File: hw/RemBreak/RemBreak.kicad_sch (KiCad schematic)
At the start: 6 parts, among them J2 Conn_02x06_Odd_Even

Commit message: updated pcb and schematics - still in progress
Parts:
- removed R3: 0R, Resistor_SMD:R_0805_2012Metric, symbol Device:R
- added J3, J5: Screw_Terminal_01x04, TerminalBlock_Phoenix:TerminalBlock_Phoenix_MPT-0,5-4-2.54_1x04_P2.54mm_Horizontal, symbol Connector:Screw_Terminal_01x04
- J2: footprint Connector_PinHeader_2.54mm:PinHeader_2x06_P2.54mm_Vertical_SMD -> dodo_conn:SAMTEC_TSM-106-01-L-DH-P-TR
- R1: now not fitted
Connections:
- net GND: now also J2.11 (Pin_11), J2.12 (Pin_12), J2.7 (Pin_7), J2.8 (Pin_8), J3.4 (Pin_4), J5.2 (Pin_2), J5.4 (Pin_4)
- net 7V5: now reaches R1.1
- net 7V5: now also J5.1 (Pin_1)
- net at R1.2: now also R2.2, J3.1 (Pin_1)
- net VEXT: now reaches R2.1
- net VEXT: now also J5.3 (Pin_3)
- net 3V3: now reaches J2.1 (Pin_1)
- net SCL: now reaches J2.10 (Pin_10)
- net 5V: now reaches J2.2 (Pin_2)
- net SW+: now reaches J2.3 (Pin_3)
- net SW-: now reaches J2.4 (Pin_4)
- net DISP_DCKI: now reaches J2.5 (Pin_5)
- net DISP_DI: now reaches J2.6 (Pin_6)
- net SDA: now reaches J2.9 (Pin_9)
- new net BUTTON: J3.3 (Pin_3)
- new net BUZZER: J3.2 (Pin_2)
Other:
- note removed: "HANDLEBARS + BOOST CONVERTER (12V)"
- note removed: "SERVO"
- moved on the sheet: J2

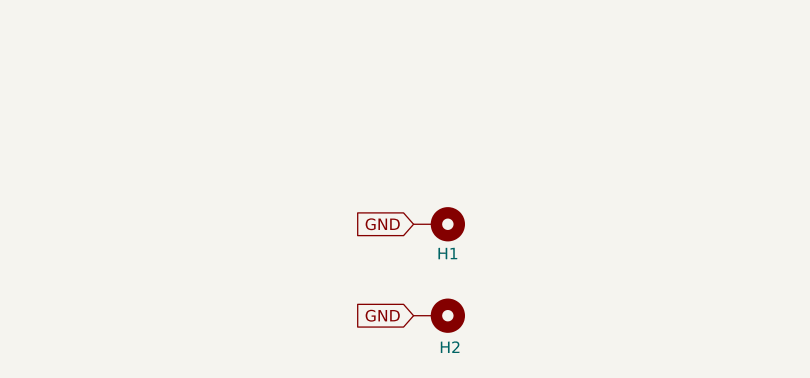
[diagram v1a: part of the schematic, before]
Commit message: changed size of the board and development of schematic
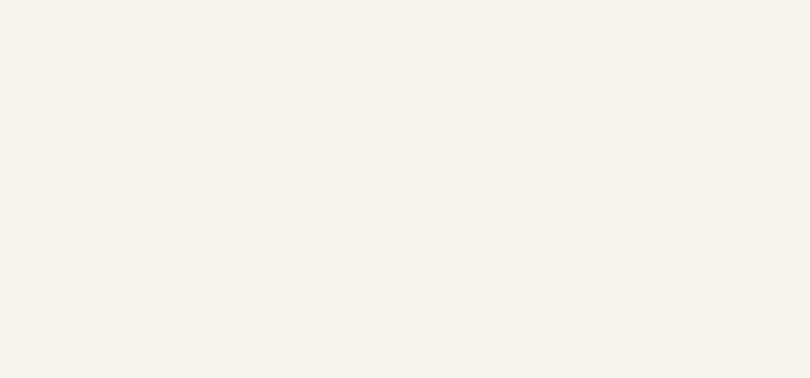
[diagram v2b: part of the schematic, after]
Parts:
- removed H1, H2: MountingHole_Pad, TestPoint:TestPoint_THTPad_2.0x2.0mm_Drill1.0mm, symbol Mechanical:MountingHole_Pad
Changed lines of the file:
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@@
-		)
-	)
-	(global_label "GND"
-		(shape input)
-		(at 153.67 175.26 180)
-		(fields_autoplaced yes)
-		(effects
-			(font
-				(size 1.27 1.27)
-			)
-			(justify right)
-		)
-		(property "Intersheetrefs" "${INTERSHEET_REFS}"
-			(at 146.8143 175.26 0)
-			(effects
-				(font
-					(size 1.27 1.27)
-				)
-				(justify right)
-				(hide yes)
-			)
-		)
-	)
-	(global_label "GND"
-		(shape input)
-		(at 153.67 185.42 180)
-		(fields_autoplaced yes)
-		(effects
-			(font
-				(size 1.27 1.27)
-			)
-			(justify right)
-		)
-		(property "Intersheetrefs" "${INTERSHEET_REFS}"
-			(at 146.8143 185.42 0)
-			(effects
-				(font
-					(size 1.27 1.27)
-				)
-				(justify right)
-				(hide yes)
-			)
 		)
 	)
@@
 	)
 	(symbol
-		(lib_id "Mechanical:MountingHole_Pad")
-		(at 156.21 175.26 270)
-		(unit 1)
-		(exclude_from_sim no)
-		(in_bom yes)
-		(on_board yes)
-		(dnp no)
-		(property "Reference" "H1"
-			(at 157.48 178.562 90)
-			(effects
-				(font
-					(size 1.27 1.27)
-				)
-			)
-		)
-		(property "Value" "MountingHole_Pad"
-			(at 157.48 179.07 90)
-			(effects
-				(font
-					(size 1.27 1.27)
-				)
-				(hide yes)
-			)
-		)
-		(property "Footprint" "TestPoint:TestPoint_THTPad_2.0x2.0mm_Drill1.0mm"
-			(at 156.21 175.26 0)
-			(effects
-				(font
-					(size 1.27 1.27)
-				)
-				(hide yes)
-			)
-		)
-		(property "Datasheet" "~"
-			(at 156.21 175.26 0)
-			(effects
-				(font
-					(size 1.27 1.27)
-				)
-				(hide yes)
-			)
-		)
-		(property "Description" "Mounting Hole with connection"
-			(at 156.21 175.26 0)
-			(effects
-				(font
-					(size 1.27 1.27)
-				)
-				(hide yes)
-			)
-		)
-		(pin "1"
-		)
-		(instances
-			(project "RemBreak"
-				(path "/e6d4ae5b-c9d7-4cbe-b288-c929fdf55a75"
-					(reference "H1")
-					(unit 1)
-				)
-			)
-		)
-	)
-	(symbol
 		(lib_id "Connector:Screw_Terminal_01x04")
 		(at 237.49 74.93 0)
@@
 					(unit 1)
 				)
-			)
-		)
-	)
-	(symbol
-		(lib_id "Mechanical:MountingHole_Pad")
-		(at 156.21 185.42 270)
-		(unit 1)
-		(exclude_from_sim no)
-		(in_bom yes)
-		(on_board yes)
-		(dnp no)
-		(property "Reference" "H2"
-			(at 157.734 188.976 90)
-			(effects
-				(font
-					(size 1.27 1.27)
-				)
-			)
-		)
-		(property "Value" "MountingHole_Pad"
-			(at 157.48 189.23 90)
-			(effects
-				(font
-					(size 1.27 1.27)
-				)
-				(hide yes)
-			)
-		)
-		(property "Footprint" "TestPoint:TestPoint_THTPad_2.0x2.0mm_Drill1.0mm"
-			(at 156.21 185.42 0)
-			(effects
-				(font
-					(size 1.27 1.27)
-				)
-				(hide yes)
-			)
-		)
-		(property "Datasheet" "~"
-			(at 156.21 185.42 0)
-			(effects
-				(font
-					(size 1.27 1.27)
-				)
-				(hide yes)
-			)
-		)
-		(property "Description" "Mounting Hole with connection"
-			(at 156.21 185.42 0)
-			(effects
-				(font
-					(size 1.27 1.27)
-				)
-				(hide yes)
-			)
-		)
-		(pin "1"
-		)
-		(instances
-			(project ""
-				(path "/e6d4ae5b-c9d7-4cbe-b288-c929fdf55a75"
-					(reference "H2")
-					(unit 1)
-				)

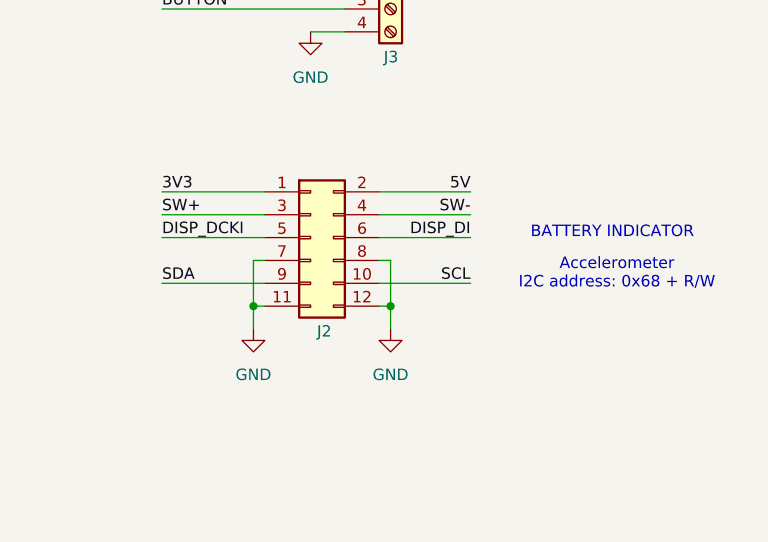
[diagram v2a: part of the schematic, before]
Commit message: added RGB LED connection - missing connections in schematics
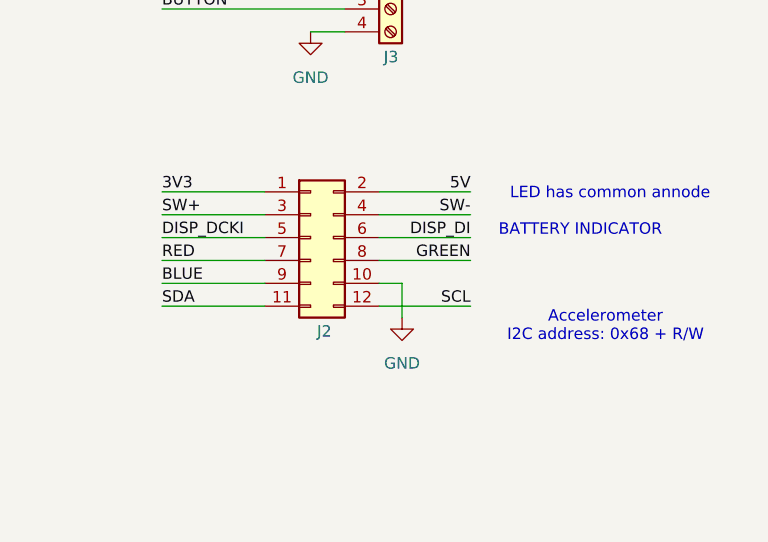
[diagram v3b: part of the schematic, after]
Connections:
- net GND: now also J2.10 (Pin_10); no longer J2.11 (Pin_11), J2.12 (Pin_12), J2.7 (Pin_7), J2.8 (Pin_8)
- net SCL: now also J2.12 (Pin_12); no longer J2.10 (Pin_10)
- net SDA: now also J2.11 (Pin_11); no longer J2.9 (Pin_9)
- new net BLUE: J2.9 (Pin_9)
- new net GREEN: J2.8 (Pin_8)
- new net RED: J2.7 (Pin_7)
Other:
- note added: "LED has common annode"

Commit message: finished schematics routing and erc passed
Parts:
- J2: footprint dodo_conn:SAMTEC_TSM-106-01-L-DH-P-TR -> chinese_modules:SAMTEC_TSM-106-01-L-DH-P-TR
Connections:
- net BUTTON is gone; now on net break_control/BUTTON: J3.3 (Pin_3)
- net SW+ is gone; now on net power_manager/VBATT: J2.3 (Pin_3)
- net 3V3 renamed +3V3
- net 5V renamed +5V
- net 7V5 renamed +7.5V
- net BLUE renamed power_manager/CHARGED (GREEN)
- net BUZZER renamed break_control/BUZZER
- net DISP_DCKI renamed DISPLAY.DCKI
- net DISP_DI renamed DISPLAY.DI
- net GREEN renamed power_switch/RUNNIG (RED)
- net RED renamed break_control/CHARGING
- net SCL renamed I2C.SCL
- net SDA renamed I2C.SDA
- net SW- renamed power_switch/ON/OFF
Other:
- sheet break_control ports: added BALARM, BUZZER, CHARGING, DISPLAY{DCKI DI}, I2C{SDA SCL}; removed I2C, PWR
- sheet power_manager ports: added BALARM, CHARGED (GREEN), CHARGING (BLUE), I2C{SDA SCL}, VBUS; removed 3V3, I2C
- sheet power_switch ports: added ON/OFF, RUNNIG (RED); removed PWR
- note added: "Potentially connect MPU6050 I2C address: 0x68 + R/W"
- note removed: "Accelerometer I2C address: 0x68 + R/W"
- note removed: "LED has common annode"
- moved on the sheet: J2, J3, J5, R1, R2

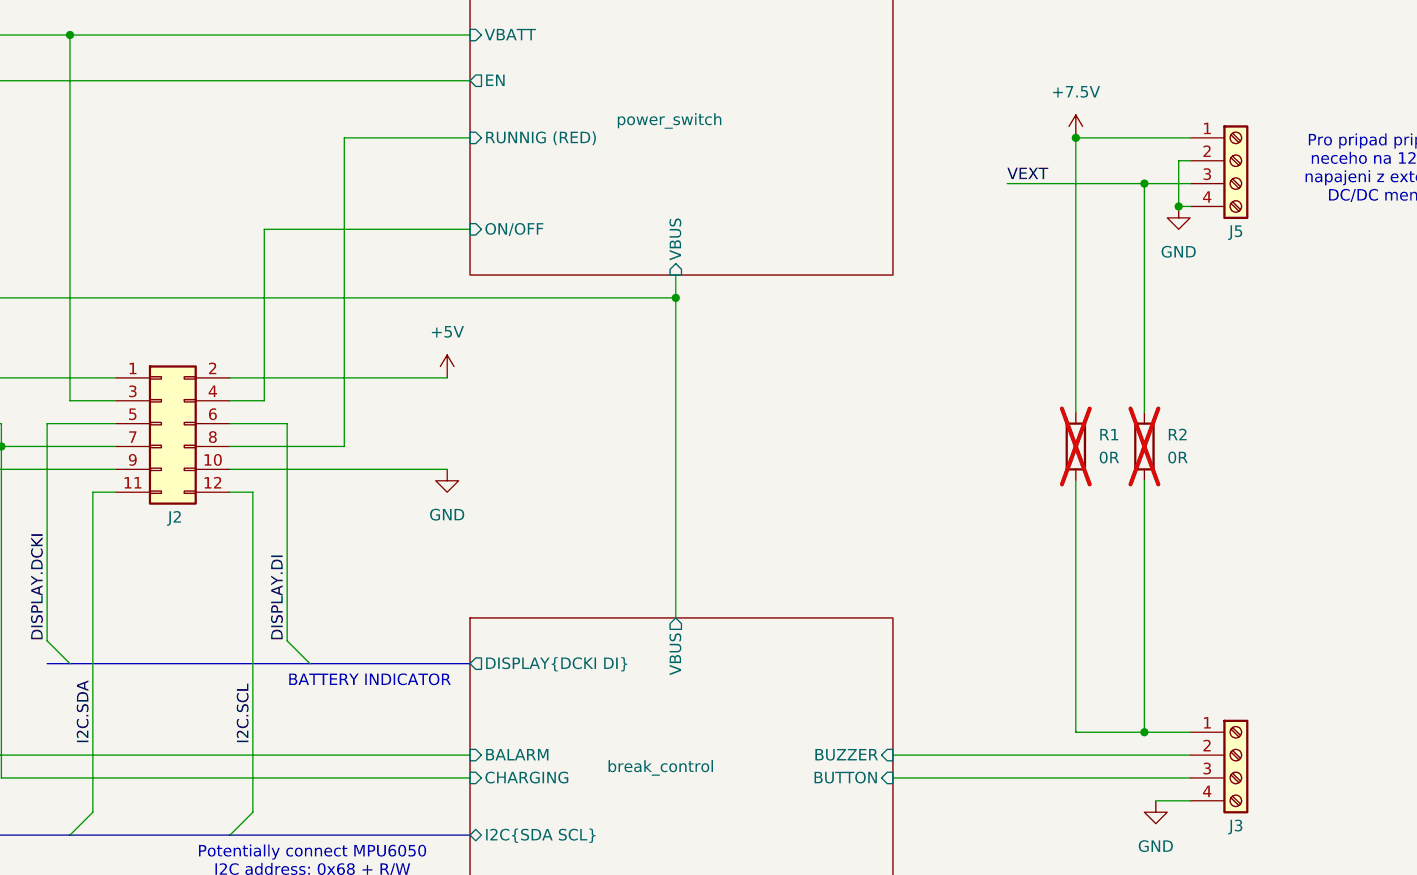
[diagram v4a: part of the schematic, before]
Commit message: regenerated anotations and used battery connector with grounding
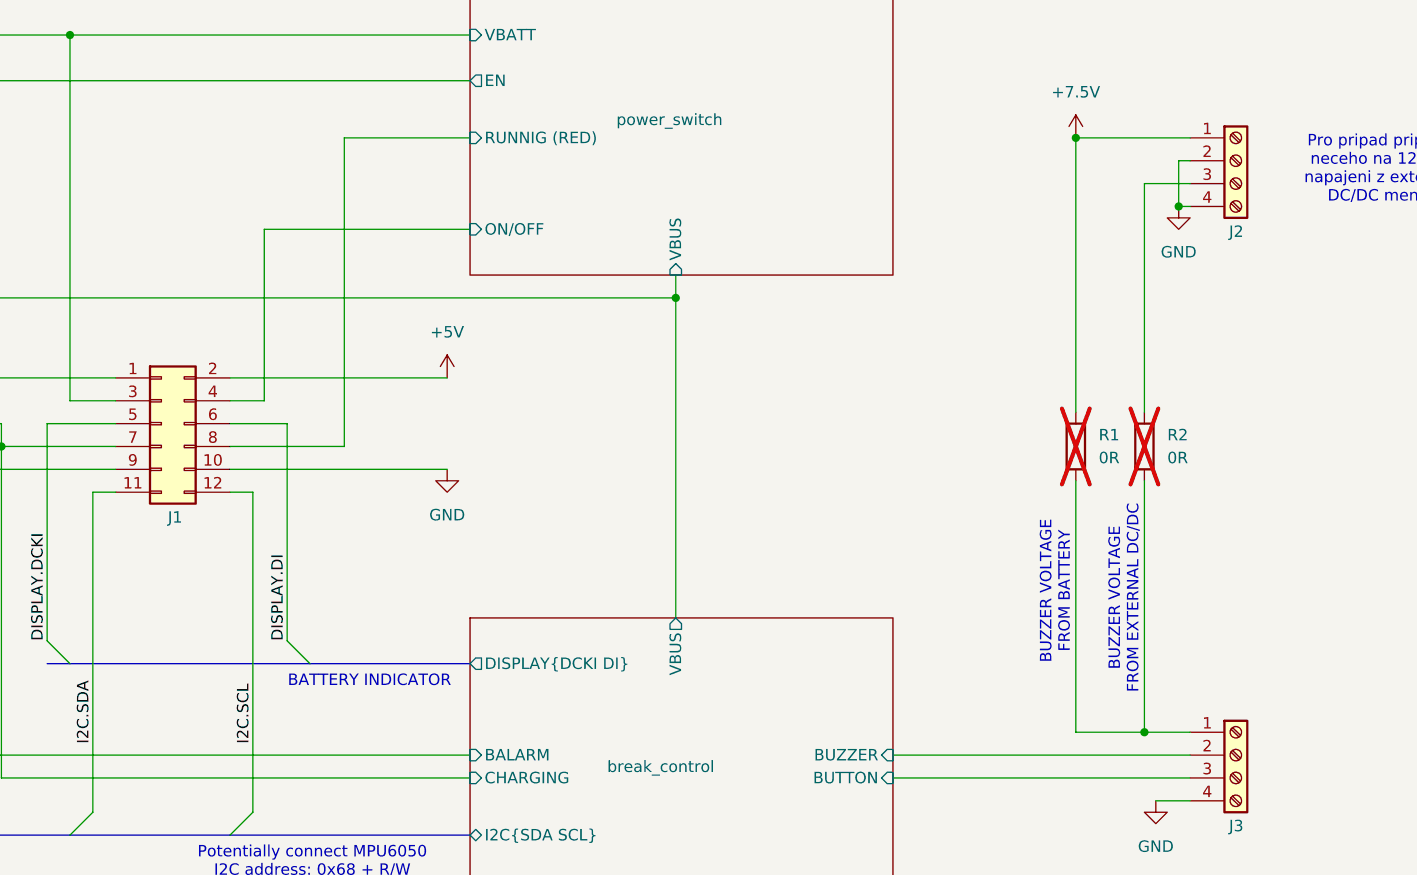
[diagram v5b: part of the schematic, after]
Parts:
- renumbered J2 to J1, J5 to J2
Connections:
- net VEXT: no longer names the net of J2.3 (Pin_3), R2.1
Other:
- note added: "BUZZER VOLTAGE FROM BATTERY"
- note added: "BUZZER VOLTAGE FROM EXTERNAL DC/DC"
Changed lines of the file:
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@@
+		)
+	)
+	(text "BUZZER VOLTAGE\nFROM BATTERY"
+		(exclude_from_sim no)
+		(at 226.314 111.506 90)
+		(effects
+			(font
+				(size 1.27 1.27)
+			)
+		)
+	)
+	(text "BUZZER VOLTAGE\nFROM EXTERNAL DC/DC"
+		(exclude_from_sim no)
+		(at 233.934 112.268 90)
+		(effects
+			(font
+				(size 1.27 1.27)
+			)
 		)
 	)
@@
 	)
 	(junction
-		(at 236.22 66.04)
-		(diameter 0)
-		(color 0 0 0 0)
-	)
-	(junction
 		(at 228.6 60.96)
 		(diameter 0)
@@
 	(wire
 		(pts
-			(xy 220.98 66.04) (xy 236.22 66.04)
-		)
-		(stroke
-			(width 0)
-			(type default)
-		)
-	)
-	(wire
-		(pts
 			(xy 119.38 100.33) (xy 119.38 135.89)
 		)
@@
 			(width 0)
 			(type default)
-		)
-	)
-	(label "VEXT"
-		(at 220.98 66.04 0)
-		(fields_autoplaced yes)
-		(effects
-			(font
-				(size 1.27 1.27)
-			)
-			(justify left bottom)
 		)
 	)
@@
 		(dnp no)
 		(fields_autoplaced yes)
-		(property "Reference" "#PWR042"
+		(property "Reference" "#PWR03"
 			(at 158.75 104.14 0)
 			(effects
@@
 			(project ""
 				(path "/e6d4ae5b-c9d7-4cbe-b288-c929fdf55a75"
-					(reference "#PWR042")
+					(reference "#PWR03")
 					(unit 1)
 				)
@@
 		(dnp no)
 		(fields_autoplaced yes)
-		(property "Reference" "#PWR04"
+		(property "Reference" "#PWR05"
 			(at 237.49 140.97 0)
 			(effects
@@
 			(project "RemBreak"
 				(path "/e6d4ae5b-c9d7-4cbe-b288-c929fdf55a75"
-					(reference "#PWR04")
+					(reference "#PWR05")
 					(unit 1)
 				)
@@
 		(dnp no)
 		(fields_autoplaced yes)
-		(property "Reference" "#PWR01"
+		(property "Reference" "#PWR06"
 			(at 240.03 74.93 0)
 			(effects
@@
 			(project "RemBreak"
 				(path "/e6d4ae5b-c9d7-4cbe-b288-c929fdf55a75"
-					(reference "#PWR01")
+					(reference "#PWR06")
 					(unit 1)
 				)
@@
 		(dnp no)
 		(fields_autoplaced yes)
-		(property "Reference" "#PWR041"
+		(property "Reference" "#PWR01"
 			(at 100.33 91.44 0)
 			(effects
@@
 			(project "RemBreak"
 				(path "/e6d4ae5b-c9d7-4cbe-b288-c929fdf55a75"
-					(reference "#PWR041")
+					(reference "#PWR01")
 					(unit 1)
 				)
@@
 		(on_board yes)
 		(dnp no)
-		(property "Reference" "J2"
+		(property "Reference" "J1"
 			(at 128.524 103.124 0)
 			(effects
@@
 			(project ""
 				(path "/e6d4ae5b-c9d7-4cbe-b288-c929fdf55a75"
-					(reference "J2")
+					(reference "J1")
 					(unit 1)
 				)
@@
 		(dnp no)
 		(fields_autoplaced yes)
-		(property "Reference" "#PWR044"
+		(property "Reference" "#PWR02"
 			(at 158.75 91.44 0)
 			(effects
@@
 			(project "RemBreak"
 				(path "/e6d4ae5b-c9d7-4cbe-b288-c929fdf55a75"
-					(reference "#PWR044")
+					(reference "#PWR02")
 					(unit 1)
 				)
@@
 		(dnp no)
 		(fields_autoplaced yes)
-		(property "Reference" "#PWR043"
+		(property "Reference" "#PWR04"
 			(at 228.6 64.77 0)
 			(effects
@@
 			(project "RemBreak"
 				(path "/e6d4ae5b-c9d7-4cbe-b288-c929fdf55a75"
-					(reference "#PWR043")
+					(reference "#PWR04")
 					(unit 1)
 				)
@@
 		(on_board yes)
 		(dnp no)
-		(property "Reference" "J5"
+		(property "Reference" "J2"
 			(at 245.618 71.374 0)
 			(effects
@@
 			(project "RemBreak"
 				(path "/e6d4ae5b-c9d7-4cbe-b288-c929fdf55a75"
-					(reference "J5")
+					(reference "J2")
 					(unit 1)
 				)
